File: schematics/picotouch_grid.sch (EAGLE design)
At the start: 137 parts, among them K1 TOUCHKEYH, K10 TOUCHKEYH, K11 TOUCHKEYH, K12 TOUCHKEYH, K13 TOUCHKEYH, K14 TOUCHKEYH, K15 TOUCHKEYH, K16 TOUCHKEYH, K17 TOUCHKEYH, K18 TOUCHKEYH, K19 TOUCHKEYH, K2 TOUCHKEYH, K20 TOUCHKEYH, K21 TOUCHKEYH, K22 TOUCHKEYH, K23 TOUCHKEYH, K24 TOUCHKEYH, K25 TOUCHKEYH, K26 TOUCHKEYH, K27 TOUCHKEYH, K28 TOUCHKEYH, K29 TOUCHKEYH, K3 TOUCHKEYH, K30 TOUCHKEYH, K31 TOUCHKEYH, K32 TOUCHKEYH, K33 TOUCHKEYH, K34 TOUCHKEYH, K35 TOUCHKEYH, K36 TOUCHKEYH, K37 TOUCHKEYH, K38 TOUCHKEYH, K39 TOUCHKEYH, K4 TOUCHKEYH, K40 TOUCHKEYH, K5 TOUCHKEYH, K6 TOUCHKEYH, K7 TOUCHKEYH, K8 TOUCHKEYH, K9 TOUCHKEYH, U1 RASPBERRY_PICOSMD

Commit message: more grid idea
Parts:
- removed J2: (no value), SparkFun-Connectors:CONN_04
- added CONN1: STEMMA_I2C_QT, adafruit_electromech:STEMMA_I2C_QT
- added J3: AUDIO-JACK-TRRS, audio_jacks_todbot:AUDIO-JACK-TRRS
- added R15: 1.8k, rcl:R-EU_R0805
- added R17: 220, rcl:R-EU_R0805
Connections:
- new net MIDI_OUT: R17.2, U1.GP20
- new net N$38: J3.RING1, R15.1
- new net N$8: J3.TIP, R17.1
- net +3V3: now also CONN1G$1.V+, R15.2; no longer J2.2
- net GND: now also CONN1G$1.GND, J3.EARTH; no longer J2.1
- net SCL: now also CONN1G$1.SCL; no longer J2.3
- net SDA: now also CONN1G$1.SDA; no longer J2.4
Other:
- note added: "GND"
- note added: "MIDI TRS-A OUT"
- note added: "RING1"
- note added: "RING2"
- note added: "TIP"

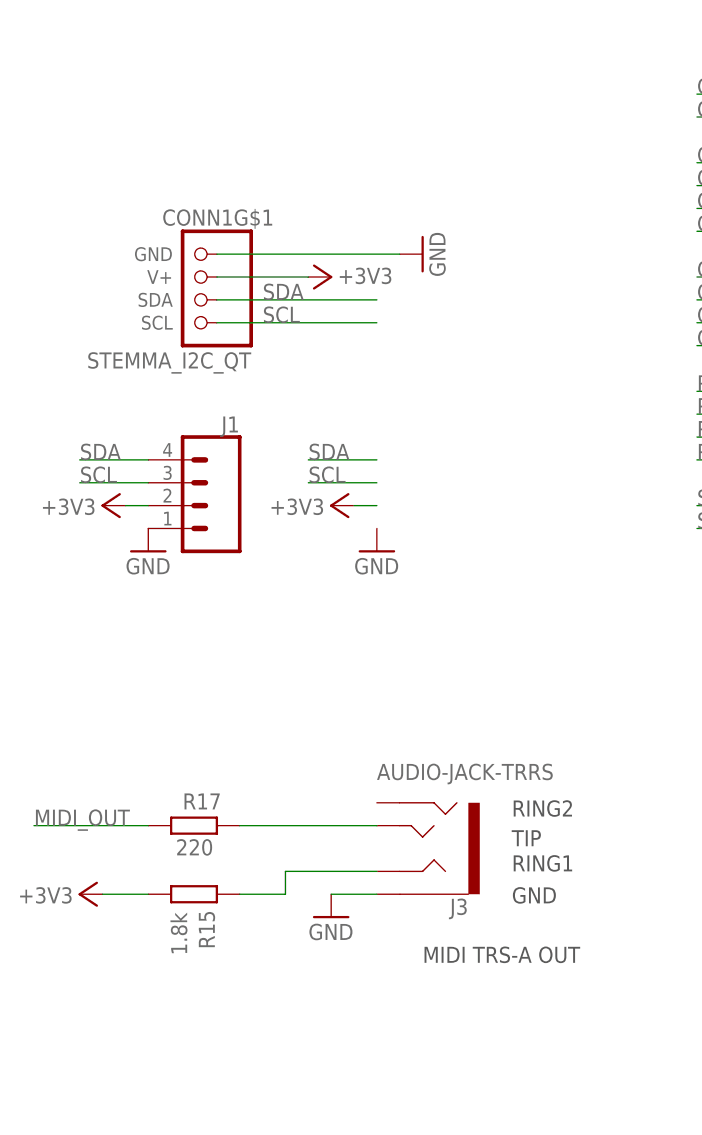
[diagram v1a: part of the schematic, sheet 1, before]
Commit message: grid idea has cutout now
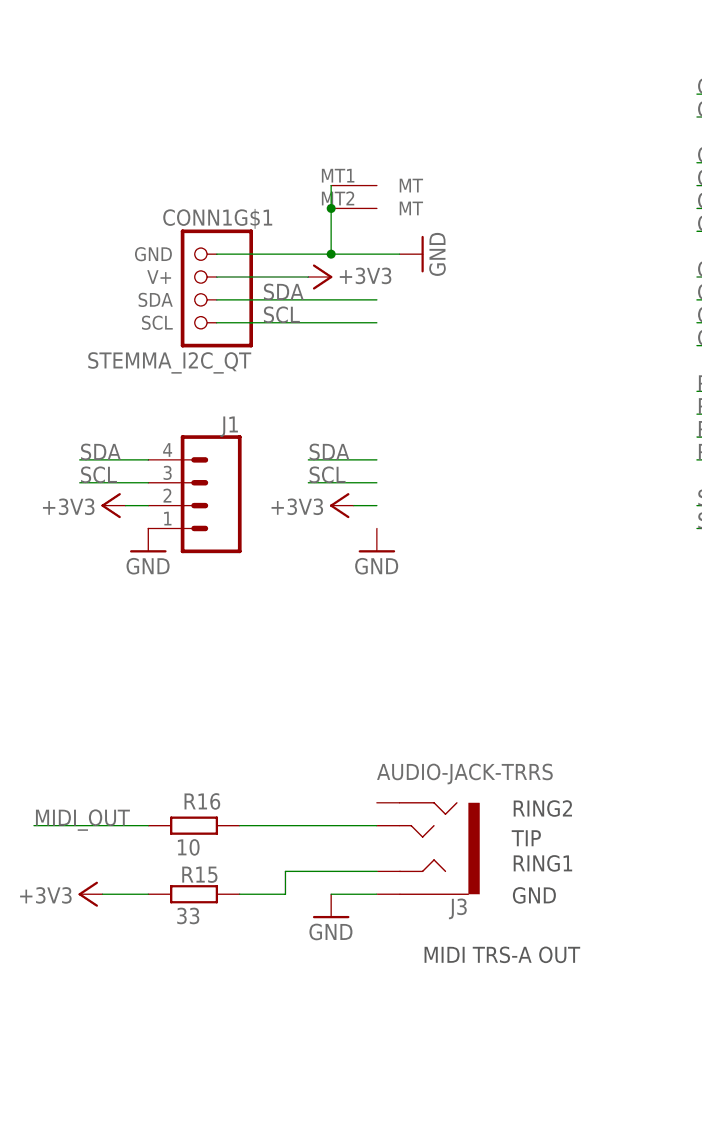
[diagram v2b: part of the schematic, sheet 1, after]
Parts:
- R15: value 1.8k -> 33
- R16: value 220 -> 10
- renumbered R17 to R16
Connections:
- net GND: now also CONN1G$2.MT, CONN1G$3.MT
